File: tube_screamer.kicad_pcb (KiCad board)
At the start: 2 copper layers, 35 parts, among them Q1 BC817, U1 TL072

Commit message: PCB layout.
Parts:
- U1: footprint Package_SO:SOIC-8-1EP_3.9x4.9mm_P1.27mm_EP2.514x3.2mm -> Package_SO:SOIC-8_3.9x4.9mm_P1.27mm
- moved R7 71.7 mm to (119.8, 140.8), turned to 180 degrees
- moved C8 64.2 mm to (111.0, 136.5), turned to 180 degrees
- moved R10 63.1 mm to (110.9, 134.4)
- moved R9 63.1 mm to (110.8, 132.3)
- moved R8 60.9 mm to (110.3, 127.6), turned to 180 degrees
- moved R6 60.7 mm to (123.2, 138.9)
- moved R3 59.0 mm to (120.0, 130.4), turned to -90 degrees
- moved R15 58.9 mm to (116.5, 118.3), turned to 180 degrees
- moved R13 58.1 mm to (109.3, 120.2), turned to 180 degrees
- moved R5 57.8 mm to (131.3, 126.8), turned to 90 degrees
- moved R17 55.8 mm to (115.8, 125.2), turned to -90 degrees
- moved C7 54.0 mm to (123.2, 140.7), turned to 180 degrees
- moved R12 52.8 mm to (108.3, 123.1), turned to -90 degrees
- moved C6 52.4 mm to (123.3, 137.1)
- moved TP5 52.4 mm to (103.0, 133.9)
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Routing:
- net 4V5: track 0.00 -> 47.8 mm, vias 0 -> 3
- net 9V: track 0.00 -> 31.0 mm, vias 0 -> 3
- net Net-(D1-A): track 0.00 -> 25.3 mm
- net Net-(D1-K): track 0.00 -> 25.2 mm
- net Net-(U1B--): track 0.00 -> 11.5 mm
- net Net-(D4-A): track 0.00 -> 10.5 mm
- net Net-(U1A-+): track 0.00 -> 8.63 mm
- net Net-(C6-Pad2): track 0.00 -> 7.53 mm
- net Net-(Q1-E): track 0.00 -> 7.08 mm
- net 0: track 0.00 -> 6.37 mm, vias 0 -> 9
- net Net-(R12-Pad1): track 0.00 -> 4.92 mm
- net Net-(R8-Pad1): track 0.00 -> 4.19 mm
- net Net-(D3-K): track 0.00 -> 4.14 mm
- net Net-(Q1-B): track 0.00 -> 3.90 mm
- net Net-(C4-Pad2): track 0.00 -> 2.64 mm
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- added copper zone on B.Cu, net 0
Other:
- board outline added: 38 x 45 mm

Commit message: PCB update.
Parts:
- added TP10: ground, TestPoint:TestPoint_Pad_2.0x2.0mm, F.Cu at (112.6, 141.1)
- added TP9: input, TestPoint:TestPoint_Pad_2.0x2.0mm, F.Cu at (116.2, 141.2)
- moved TP4 13.4 mm to (103.2, 141.9)
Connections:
- R7 pad 2: unconnected-(R7-Pad2) -> Net-(R7-Pad2)
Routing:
- net Net-(R7-Pad2): track 0.00 -> 2.92 mm
- net 0: vias 9 -> 10

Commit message: Updated schematic
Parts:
- removed C8: 10u, Capacitor_SMD:C_0603_1608Metric_Pad1.08x0.95mm_HandSolder
- removed D4: 1N4148WS, Diode_SMD:D_SOD-323
- removed R10, R9: 47k, Resistor_SMD:R_0603_1608Metric_Pad0.98x0.95mm_HandSolder
- removed R5: 4.7k, Resistor_SMD:R_0603_1608Metric_Pad0.98x0.95mm_HandSolder
- removed R8: 510, Resistor_SMD:R_0603_1608Metric_Pad0.98x0.95mm_HandSolder
- removed TP3: Red Error LED, TestPoint:TestPoint_Pad_2.0x2.0mm
- removed TP4, TP6: ground, TestPoint:TestPoint_Pad_2.0x2.0mm
- removed TP5: Power Supply, TestPoint:TestPoint_Pad_2.0x2.0mm
- added C11: 10u, Capacitor_SMD:C_0603_1608Metric_Pad1.08x0.95mm_HandSolder, F.Cu at (69.5, 126.2)
- added C12: 100n, Capacitor_SMD:C_0603_1608Metric_Pad1.08x0.95mm_HandSolder, F.Cu at (69.5, 128.8)
- added C13: 10u, Capacitor_SMD:C_0603_1608Metric_Pad1.08x0.95mm_HandSolder, F.Cu at (73.8, 118.7)
- added C14: 10u, Capacitor_SMD:C_0603_1608Metric_Pad1.08x0.95mm_HandSolder, F.Cu at (73.8, 121.2)
- added Q2: MMBT5551, Package_TO_SOT_SMD:SOT-23, F.Cu at (69.7, 132.4)
- added Q3: MMBT5551, Package_TO_SOT_SMD:SOT-23, F.Cu at (69.7, 137.0)
- added R11: 100, Resistor_SMD:R_0603_1608Metric_Pad0.98x0.95mm_HandSolder, F.Cu at (78.2, 121.2)
- added R14: 1k, Resistor_SMD:R_0603_1608Metric_Pad0.98x0.95mm_HandSolder, F.Cu at (78.2, 123.7)
- added R16: 1k, Resistor_SMD:R_0603_1608Metric_Pad0.98x0.95mm_HandSolder, F.Cu at (78.2, 126.2)
- added R18: 1k, Resistor_SMD:R_0603_1608Metric_Pad0.98x0.95mm_HandSolder, F.Cu at (78.2, 128.8)
- added R19: 510k, Resistor_SMD:R_0603_1608Metric_Pad0.98x0.95mm_HandSolder, F.Cu at (82.5, 118.7)
- added R20: 10k, Resistor_SMD:R_0603_1608Metric_Pad0.98x0.95mm_HandSolder, F.Cu at (82.5, 121.2)
- added R21: 10k, Resistor_SMD:R_0603_1608Metric_Pad0.98x0.95mm_HandSolder, F.Cu at (82.5, 123.7)
- added R22: 10k, Resistor_SMD:R_0603_1608Metric_Pad0.98x0.95mm_HandSolder, F.Cu at (82.5, 126.2)
- added R23: 10k, Resistor_SMD:R_0603_1608Metric_Pad0.98x0.95mm_HandSolder, F.Cu at (82.5, 128.8)
- added RV2: 20k, Potentiometer_THT:Potentiometer_Alpha_RD901F-40-00D_Single_Vertical, F.Cu at (54.2, 121.9)
- added RV3: 100k, Potentiometer_THT:Potentiometer_Alpha_RD901F-40-00D_Single_Vertical, F.Cu at (54.2, 135.8)
- added TP11: input, TestPoint:TestPoint_Pad_2.0x2.0mm, F.Cu at (74.2, 132.0)
- added TP12: ground, TestPoint:TestPoint_Pad_2.0x2.0mm, F.Cu at (74.2, 136.1)
- C3: value 51p -> 47p
- C6: value 220p -> 220n
- C7: value 220n -> 1u
- Q1: value BC817 -> MMBT5551
- R12: value 1000k -> 1 Meg
- R15: value 470k -> 510k
- R4: value 10k -> 1k
- R6: value 680k -> 1k
- R7: value 1k -> 220
- TP9: value input -> output
- moved C4 58.6 mm to (69.5, 118.7), turned to 0 degrees
- moved C7 56.4 mm to (69.5, 123.7), turned to 0 degrees
- moved C6 56.2 mm to (69.5, 121.2)
- moved R4 55.6 mm to (73.8, 126.2), turned to 0 degrees
- moved D3 52.0 mm to (78.4, 134.4)
- moved R6 50.5 mm to (73.8, 128.8)
- moved D2 47.8 mm to (78.4, 131.5), turned to 0 degrees
- moved R7 47.2 mm to (78.2, 118.7), turned to 0 degrees
- moved R3 46.7 mm to (73.8, 123.7), turned to 0 degrees
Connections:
- C4 pad 1: Net-(D1-A) -> 0
- C5 pad 1: Net-(D3-K) -> Net-(C4-Pad2)
- C6 pad 1: Net-(U1B--) -> Net-(C6-Pad1)
- C7 pad 1: Net-(C6-Pad2) -> Net-(C7-Pad1)
- R4 pad 2: Net-(D3-K) -> Net-(D1-A)
- R6 pad 1: Net-(U1B--) -> Net-(C7-Pad1)
- R6 pad 2: Net-(C6-Pad2) -> Net-(U1B--)
- R7 pad 1: Net-(C7-Pad2) -> Net-(C6-Pad2)
- R7 pad 2: Net-(R7-Pad2) -> 0
- RV1 pad 1: unconnected-(RV1-Pad1) -> Net-(D1-A)
- TP9 pad 1: Net-(R7-Pad2) -> Net-(C11-Pad2)
- U1 pad 7: Net-(C6-Pad2) -> Net-(C7-Pad1)
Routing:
- net (no net): track 0.00 -> 14.7 mm
- net Net-(D4-A): track 10.5 -> 0.00 mm
- net Net-(C7-Pad1): track 0.00 -> 7.53 mm
- net Net-(C6-Pad2): track 7.53 -> 0.00 mm
- net Net-(R8-Pad1): track 4.19 -> 0.00 mm
- net Net-(D3-K): track 4.14 -> 0.00 mm
- net Net-(C4-Pad2): track 2.64 -> 6.78 mm
- net Net-(R7-Pad2): track 2.92 -> 0.00 mm
- net Net-(C11-Pad2): track 0.00 -> 2.92 mm

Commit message: Updated schematic and layout.
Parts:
- TP10, TP11, TP12, TP7, TP8, TP9: footprint TestPoint:TestPoint_Pad_2.0x2.0mm -> TestPoint:TestPoint_THTPad_2.5x2.5mm_Drill1.2mm
- moved RV3 104.0 mm to (152.5, 102.0), turned to -90 degrees
- moved RV2 78.4 mm to (132.5, 119.0), turned to -90 degrees
- moved C13 71.8 mm to (145.5, 122.3)
- moved C14 71.8 mm to (145.5, 124.8)
- moved R3 71.8 mm to (145.5, 127.3)
- moved R4 71.8 mm to (145.5, 129.8)
- moved R6 71.8 mm to (145.5, 132.3)
- moved Q2 71.8 mm to (141.4, 136.0)
- moved Q3 71.8 mm to (141.4, 140.6)
- moved R11 71.8 mm to (149.8, 124.8)
- moved R14 71.8 mm to (149.8, 127.3)
- moved R16 71.8 mm to (149.8, 129.8)
- moved R18 71.8 mm to (149.8, 132.3)
- moved R19 71.8 mm to (154.2, 122.3)
- moved R20 71.8 mm to (154.2, 124.8)
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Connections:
- RV1 pad 1: Net-(D1-A) -> Net-(D1-K)
- RV1 pad 3: Net-(D1-K) -> Net-(D1-A)
- RV3 pad 1: Net-(R14-Pad1) -> 0
- RV3 pad 3: 0 -> Net-(R14-Pad1)
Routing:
- net 4V5: track 47.8 -> 32.3 mm
- net (no net): track 14.7 -> 0.00 mm
- net Net-(D1-K): track 25.2 -> 33.2 mm
- net Net-(C7-Pad1): track 7.53 -> 0.05 mm
- net 9V: track 31.0 -> 26.9 mm, vias 3 -> 2
- net Net-(U1B--): track 11.5 -> 7.57 mm
- net Net-(U1A-+): track 8.63 -> 5.51 mm
- net Net-(C11-Pad2): track 2.92 -> 0.23 mm
- net 0: track 6.37 -> 4.19 mm, vias 10 -> 4
- net Net-(C7-Pad2): track 1.67 -> 0.00 mm
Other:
- board size 38 x 45 mm -> 61 x 45 mm

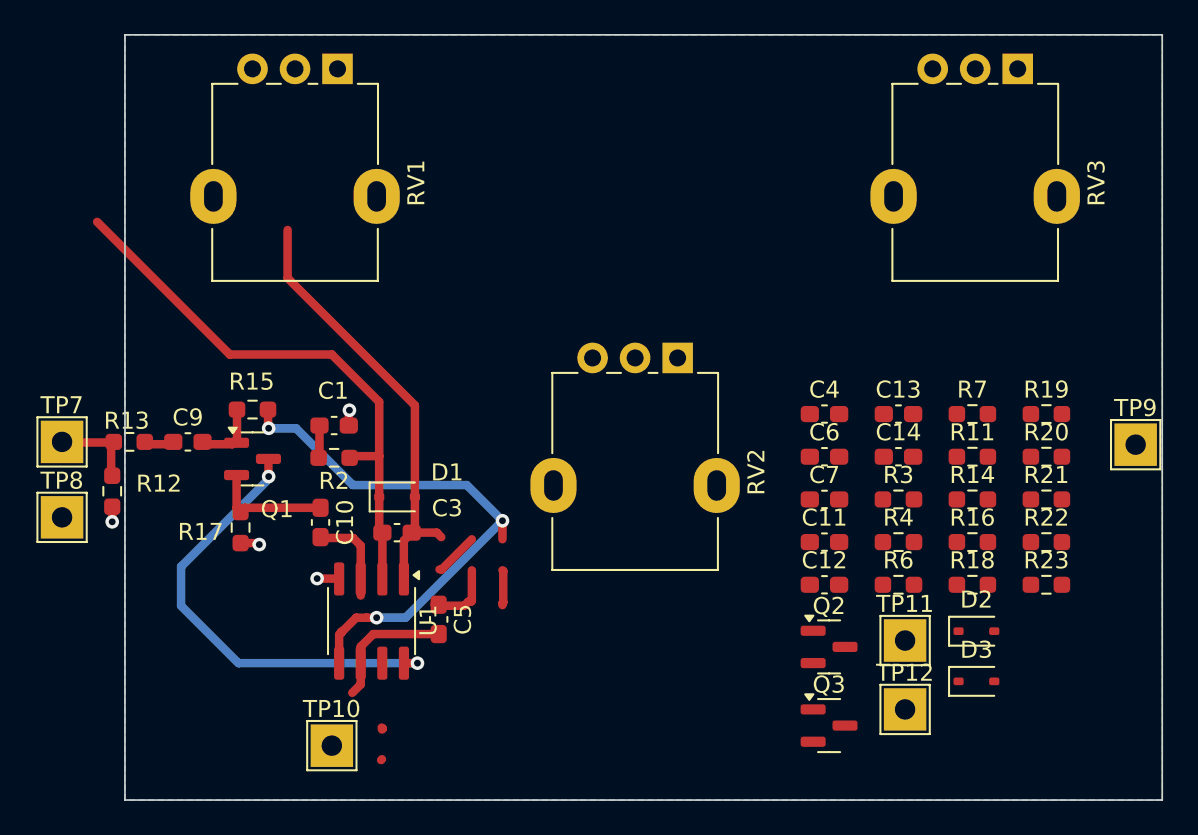
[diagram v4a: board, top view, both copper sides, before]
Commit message: poredjani potenciometri, layout na pola puta
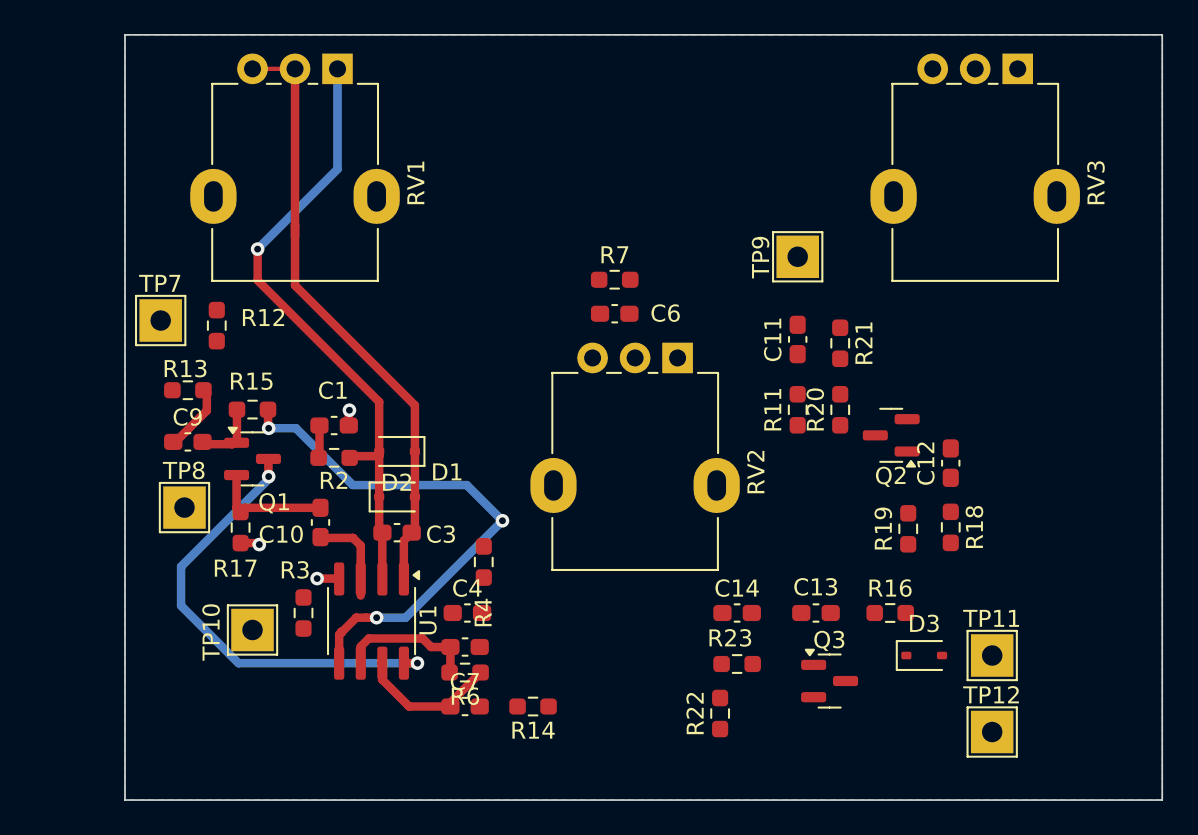
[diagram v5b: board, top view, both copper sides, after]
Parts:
- moved D2 35.7 mm to (116.0, 124.5), turned to 180 degrees
- moved R3 35.6 mm to (110.5, 134.0), turned to -90 degrees
- moved R14 28.6 mm to (124.0, 139.5), turned to 180 degrees
- moved R6 26.0 mm to (120.0, 137.5), turned to 180 degrees
- moved R4 24.4 mm to (121.1, 131.0), turned to 90 degrees
- moved C7 24.4 mm to (120.0, 139.5)
- moved C4 24.0 mm to (120.1, 134.0)
- moved TP9 22.7 mm to (139.6, 113.0), turned to 90 degrees
- moved R7 22.5 mm to (128.8, 114.4)
- moved R22 21.7 mm to (135.0, 139.9), turned to 90 degrees
- moved R23 18.8 mm to (136.0, 137.0)
- moved R21 15.2 mm to (142.1, 118.1), turned to -90 degrees
- moved C6 14.9 mm to (128.8, 116.4), turned to 180 degrees
- moved C14 13.2 mm to (136.0, 134.0)
- moved Q2 13.0 mm to (145.1, 123.5), turned to 180 degrees
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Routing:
- net Net-(D1-A): track 25.7 -> 36.4 mm
- net Net-(C7-Pad1): track 0.05 -> 8.41 mm
- net Net-(C4-Pad2): track 6.78 -> 0.00 mm
- net Net-(R12-Pad1): track 4.92 -> 0.00 mm
- net Net-(D1-K): track 33.2 -> 36.8 mm, vias 0 -> 1
- net Net-(D3-A): track 2.09 -> 0.00 mm
- net Net-(C9-Pad1): track 1.87 -> 3.89 mm
- net 4V5: track 32.3 -> 31.2 mm
- net 0: track 4.19 -> 3.30 mm, vias 4 -> 3
- net Net-(U1B--): track 7.57 -> 8.17 mm

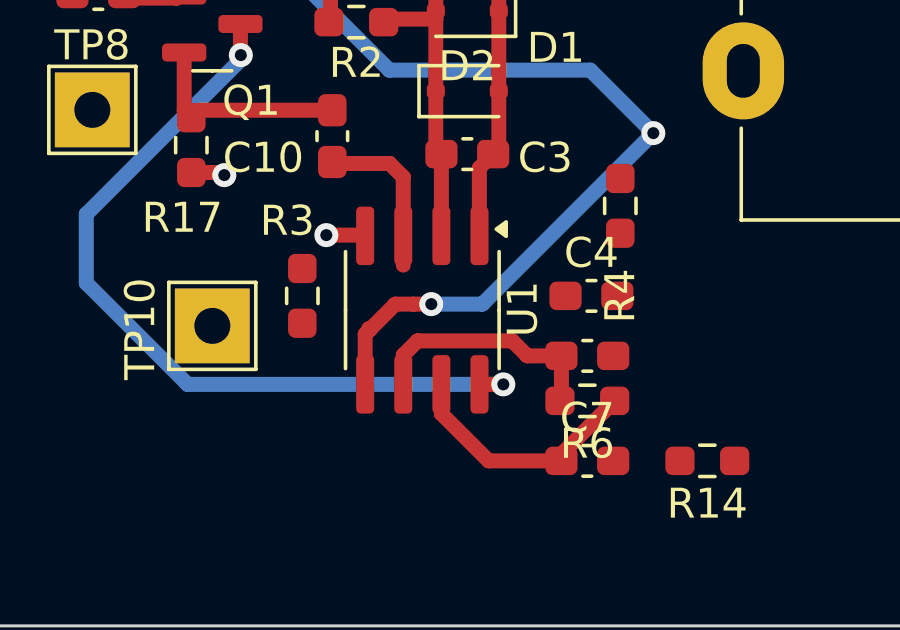
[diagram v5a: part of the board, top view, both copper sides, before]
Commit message: Changed opamp to NE5532, basic LCSC part.
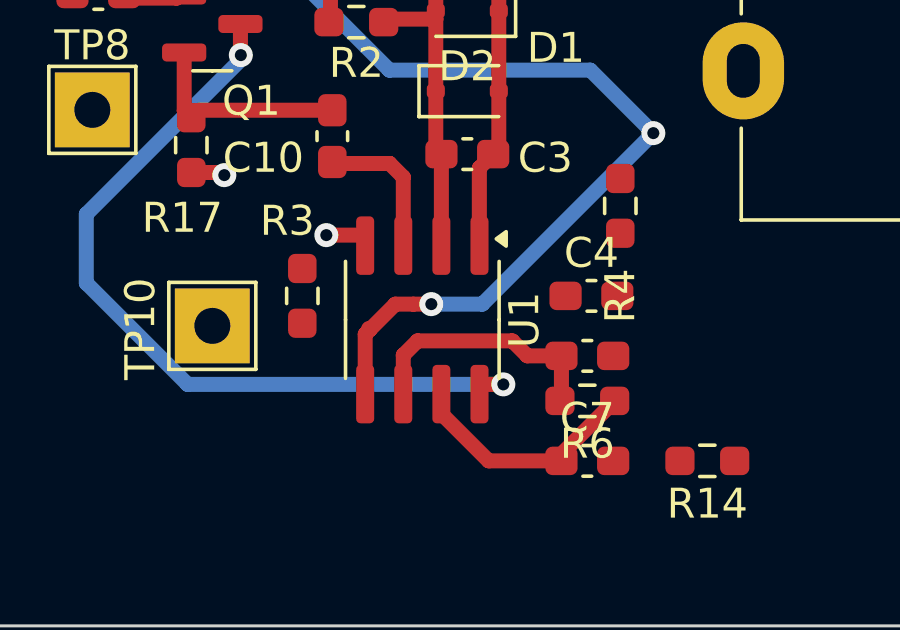
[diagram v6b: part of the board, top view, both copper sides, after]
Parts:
- U1: value TL072 -> NE5532
- moved U1 0.33 mm to (114.5, 134.8)

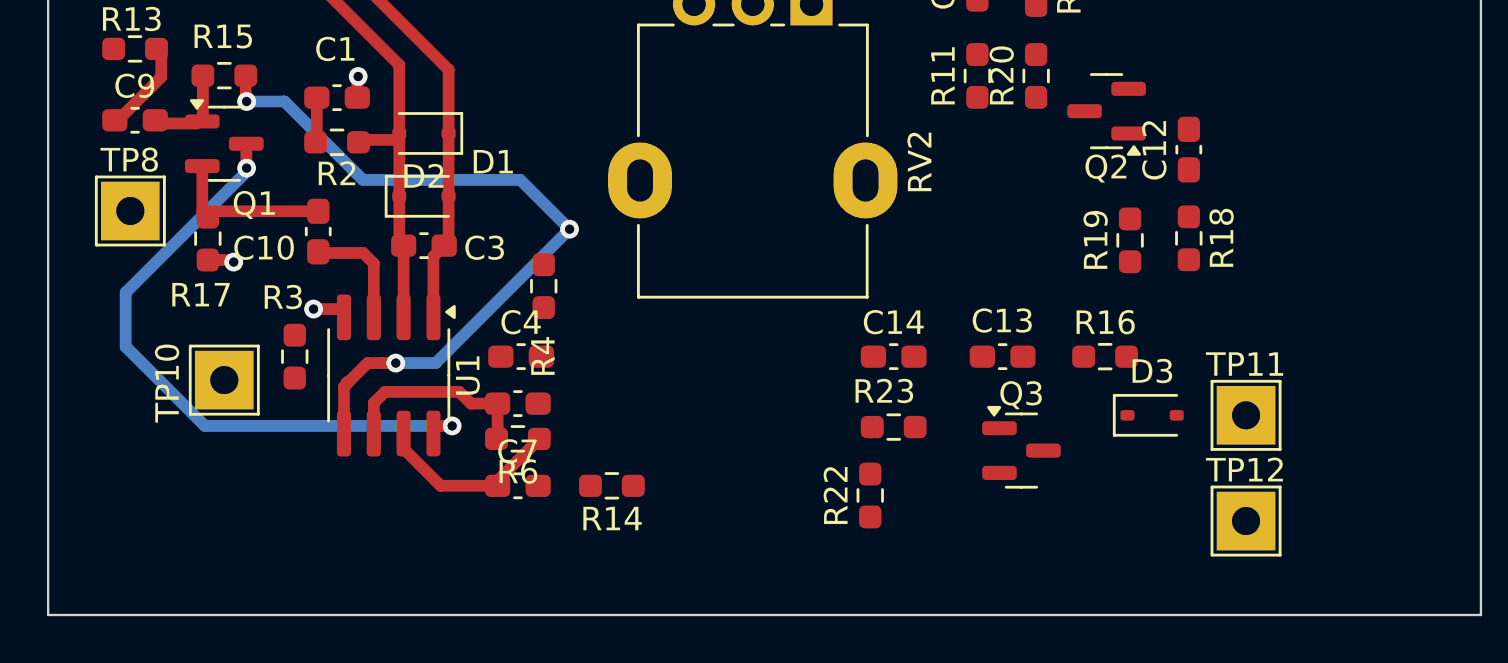
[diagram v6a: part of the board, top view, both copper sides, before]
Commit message: Added switch connectors.
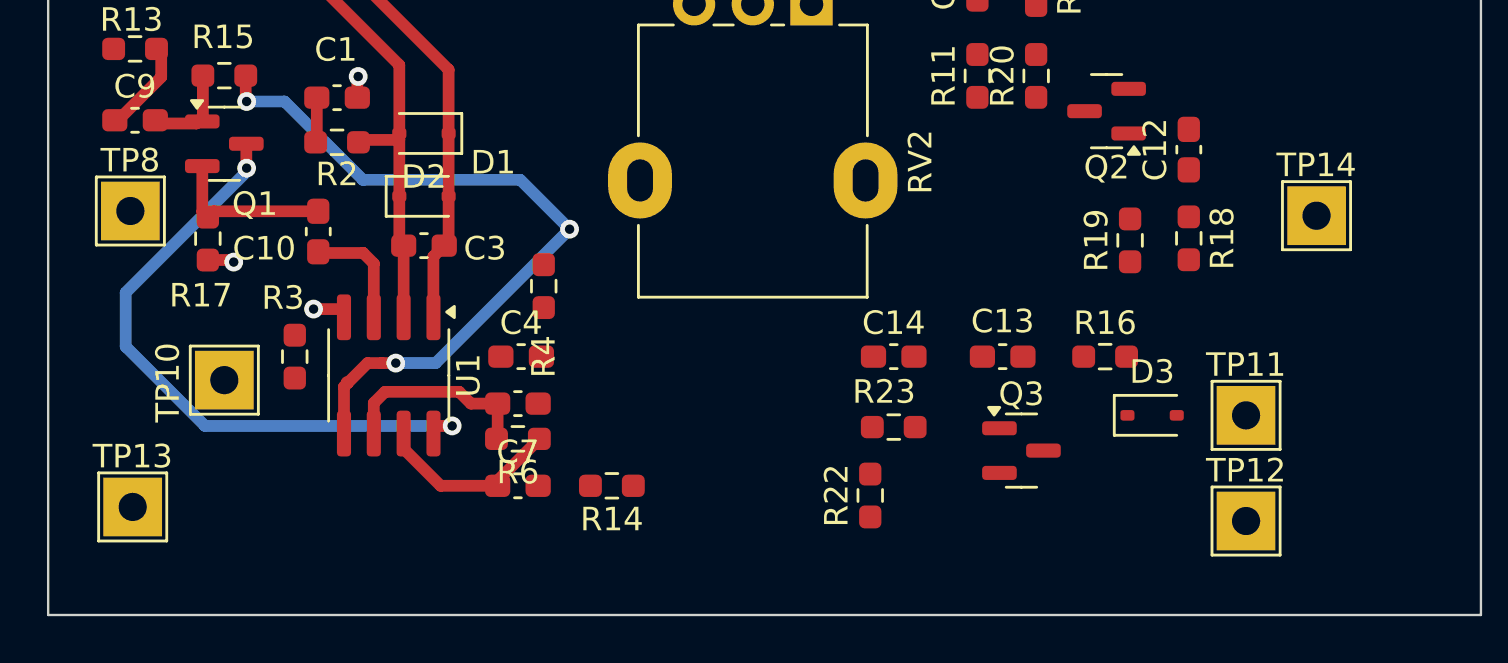
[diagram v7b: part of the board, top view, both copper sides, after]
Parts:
- added TP13: bypass_in, TestPoint:TestPoint_THTPad_2.5x2.5mm_Drill1.2mm, F.Cu at (103.6, 140.4)
- added TP14: bypass_out, TestPoint:TestPoint_THTPad_2.5x2.5mm_Drill1.2mm, F.Cu at (154.0, 128.0)
